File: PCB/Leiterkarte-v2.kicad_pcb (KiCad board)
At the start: 4 copper layers, 69.2 x 70 mm, 59 parts

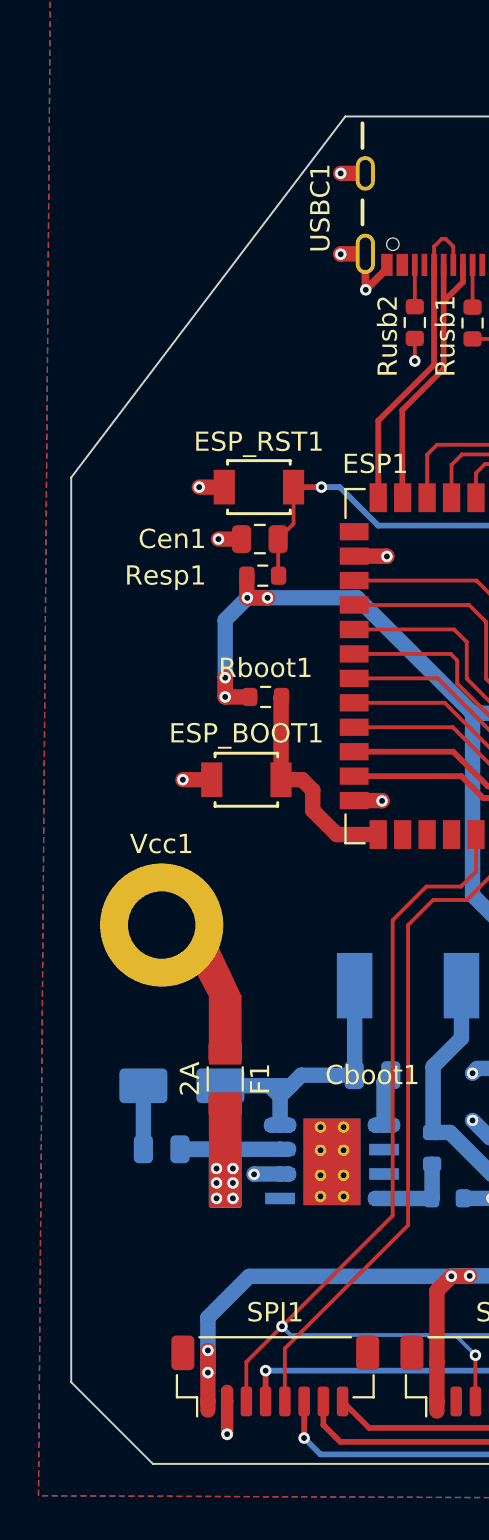
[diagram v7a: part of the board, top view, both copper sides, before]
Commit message: Changed buttons footprint; Changed buttons LCSC component due to shortage; Updated components rotation for JLCPCB;
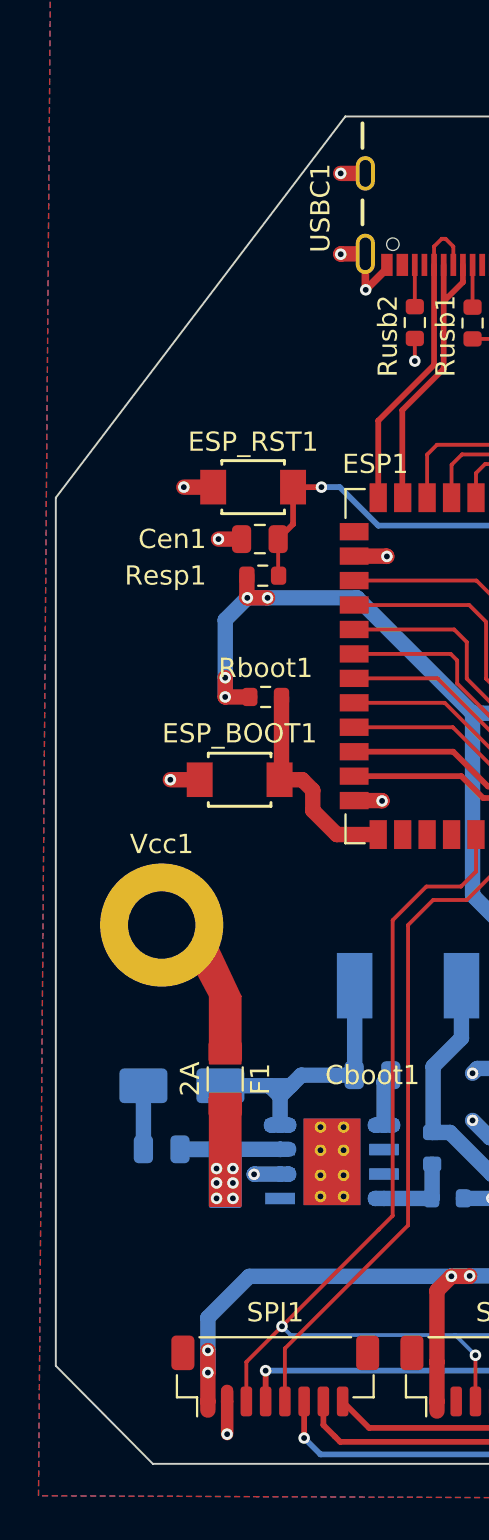
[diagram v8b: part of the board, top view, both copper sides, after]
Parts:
- moved ESP_BOOT1 0.35 mm to (94.3, 82.7)
- moved ESP_RST1 0.30 mm to (95.0, 67.5)
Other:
- board size 69.2 x 70 mm -> 70 x 70 mm
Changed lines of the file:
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@@
 		(tags "resistor")
 		(property "Reference" "Rbtn1"
-			(at 4.325 0 360)
+			(at 4.325 0 0)
 			(layer "F.SilkS")
 			(effects
@@
 		)
 		(property "Value" "10k"
-			(at 0 1.43 360)
+			(at 0 1.43 0)
 			(layer "F.Fab")
 			(effects
@@
 		)
 		(fp_text user "${REFERENCE}"
-			(at 0 0 360)
+			(at 0 0 0)
 			(layer "F.Fab")
 			(effects
@@
 		(tags "resistor")
 		(property "Reference" "Rbtn3"
-			(at -4.35 0 360)
+			(at -4.35 0 0)
 			(layer "F.SilkS")
 			(effects
@@
 		)
 		(property "Value" "10k"
-			(at 0 1.43 360)
+			(at 0 1.43 0)
 			(layer "F.Fab")
 			(effects
@@
 		)
 		(fp_text user "${REFERENCE}"
-			(at 0 0 360)
+			(at 0 0 0)
 			(layer "F.Fab")
 			(effects
@@
 	(footprint "button:small_button"
 		(layer "F.Cu")
-		(at 95.35 67.5)
+		(at 95.05 67.5)
 		(tags "B3U-1000P-B ")
 		(property "Reference" "ESP_RST1"
@@
 		)
 		(fp_line
-			(start -2.55 -1.104)
+			(start -2.9 -1.104)
 			(end -1.754 -1.104)
 			(stroke
@@
 		)
 		(fp_line
-			(start -2.55 1.104)
-			(end -2.55 -1.104)
+			(start -2.9 1.104)
+			(end -2.9 -1.104)
 			(stroke
 				(width 0.1524)
@@
 		)
 		(fp_line
-			(start -2.55 1.104)
+			(start -2.9 1.104)
 			(end -1.754 1.104)
 			(stroke
@@
 		)
 		(fp_line
-			(start 2.55 -1.104)
+			(start 2.9 -1.104)
 			(end 1.754 -1.104)
 			(stroke
@@
 		)
 		(fp_line
-			(start 2.55 -1.104)
-			(end 2.55 1.104)
+			(start 2.9 -1.104)
+			(end 2.9 1.104)
 			(stroke
 				(width 0.1524)
@@
 		)
 		(fp_line
-			(start 2.55 1.104)
+			(start 2.9 1.104)
 			(end 1.754 1.104)
 			(stroke
@@
 		)
 		(pad "1" smd rect
-			(at -1.8 0)
-			(size 1.1 1.8)
+			(at -2.075 0)
+			(size 1.35 1.8)
 			(layers "F.Cu" "F.Paste" "F.Mask")
 			(net 2 "GND")
@@
 		)
 		(pad "2" smd rect
-			(at 1.8 0)
-			(size 1.1 1.8)
+			(at 2.075 0)
+			(size 1.35 1.8)
 			(layers "F.Cu" "F.Paste" "F.Mask")
 			(net 23 "Net-(ESP1-EN)")
@@
 			(pintype "passive")
 		)
-		(model "${KIPRJMOD}/button/small_button.STEP"
-			(offset
-				(xyz 0 0 0)
-			)
-			(scale
-				(xyz 1 1 1)
-			)
-			(rotate
-				(xyz -90 0 0)
-			)
-		)
 	)
 	(footprint "Resistor_SMD:R_0603_1608Metric"
@@
 		(tags "resistor")
 		(property "Reference" "Rbtn2"
-			(at 4.35 0 360)
+			(at 4.35 0 0)
 			(layer "F.SilkS")
 			(effects
@@
 		)
 		(property "Value" "10k"
-			(at 0 1.43 360)
+			(at 0 1.43 0)
 			(layer "F.Fab")
 			(effects
@@
 		)
 		(fp_text user "${REFERENCE}"
-			(at 0 0 360)
+			(at 0 0 0)
 			(layer "F.Fab")
 			(effects
@@
 	(footprint "button:small_button"
 		(layer "F.Cu")
-		(at 94.7 82.7)
+		(at 94.35 82.7)
 		(tags "B3U-1000P-B ")
 		(property "Reference" "ESP_BOOT1"
@@
 		)
 		(fp_line
-			(start -2.55 -1.104)
+			(start -2.9 -1.104)
 			(end -1.754 -1.104)
 			(stroke
@@
 		)
 		(fp_line
-			(start -2.55 1.104)
-			(end -2.55 -1.104)
+			(start -2.9 1.104)
+			(end -2.9 -1.104)
 			(stroke
 				(width 0.1524)
@@
 		)
 		(fp_line
-			(start -2.55 1.104)
+			(start -2.9 1.104)
 			(end -1.754 1.104)
 			(stroke
@@
 		)
 		(fp_line
-			(start 2.55 -1.104)
+			(start 2.9 -1.104)
 			(end 1.754 -1.104)
 			(stroke
@@
 		)
 		(fp_line
-			(start 2.55 -1.104)
-			(end 2.55 1.104)
+			(start 2.9 -1.104)
+			(end 2.9 1.104)
 			(stroke
 				(width 0.1524)
@@
 		)
 		(fp_line
-			(start 2.55 1.104)
+			(start 2.9 1.104)
 			(end 1.754 1.104)
 			(stroke
@@
 		)
 		(pad "1" smd rect
-			(at -1.8 0)
-			(size 1.1 1.8)
+			(at -2.075 0)
+			(size 1.35 1.8)
 			(layers "F.Cu" "F.Paste" "F.Mask")
 			(net 2 "GND")
@@
 		)
 		(pad "2" smd rect
-			(at 1.8 0)
-			(size 1.1 1.8)
+			(at 2.075 0)
+			(size 1.35 1.8)
 			(layers "F.Cu" "F.Paste" "F.Mask")
 			(net 64 "Net-(ESP1-IO0)")
@@
 			(pintype "passive")
 		)
-		(model "${KIPRJMOD}/button/small_button.STEP"
-			(offset
-				(xyz 0 0 0)
-			)
-			(scale
-				(xyz 1 1 1)
-			)
-			(rotate
-				(xyz -90 0 0)
-			)
-		)
 	)
 	(footprint "Resistor_SMD:R_0603_1608Metric"
@@
 	)
 	(gr_line
+		(start 84.8 68.05)
+		(end 84.8 113.15)
+		(stroke
+			(width 0.1)
+			(type default)
+		)
+		(layer "Edge.Cuts")
+	)
+	(gr_line
 		(start 89.842641 118.242641)
 		(end 154.842641 118.242641)
@@
 	)
 	(gr_line
-		(start 85.6 67)
+		(start 84.8 68.05)
 		(end 99.842641 48.242641)
 		(stroke
@@
 	)
 	(gr_line
-		(start 85.6 114)
+		(start 84.8 113.15)
 		(end 89.842641 118.242641)
 		(stroke
@@
 	)
 	(gr_line
-		(start 85.6 114)
-		(end 85.6 67)
-		(stroke
-			(width 0.1)
-			(type default)
-		)
-		(layer "Edge.Cuts")
-	)
-	(gr_line
 		(start 93.6 90.25)
 		(end 93.6 118.25)
@@
 		(layer "User.1")
 	)
+	(gr_line
+		(start 85.6 114)
+		(end 85.6 67)
+		(stroke
+			(width 0.1)
+			(type default)
+		)
+		(layer "User.1")
+	)
 	(gr_text "FOW"
 		(at 149.95 88.25 90)
@@
 	)
 	(segment
-		(start 92.9 82.7)
-		(end 91.4 82.7)
-		(width 0.8)
-		(layer "F.Cu")
-		(net 2)
-	)
-	(segment
 		(start 124.75 76.8)
 		(end 126.2 76.8)
@@
 	)
 	(segment
+		(start 92.275 82.7)
+		(end 90.75 82.7)
+		(width 0.8)
+		(layer "F.Cu")
+		(net 2)
+	)
+	(segment
 		(start 102 56.15)
 		(end 100.9 57.25)
@@
 	)
 	(segment
-		(start 93.55 67.5)
-		(end 92.25 67.5)
-		(width 0.8)
-		(layer "F.Cu")
-		(net 2)
-	)
-	(segment
 		(start 122.3 63.7625)
 		(end 122.3 63.3)
@@
 	)
 	(segment
+		(start 92.975 67.5)
+		(end 91.45 67.5)
+		(width 0.8)
+		(layer "F.Cu")
+		(net 2)
+	)
+	(segment
 		(start 109.52 51.2)
 		(end 108.2 51.2)
@@
 	)
 	(via
-		(at 92.25 67.5)
+		(at 136.95 68)
 		(size 0.6)
 		(drill 0.3)
@@
 	)
 	(via
-		(at 136.95 68)
+		(at 91.45 67.5)
 		(size 0.6)
 		(drill 0.3)
@@
 	)
 	(via
-		(at 91.4 82.7)
+		(at 90.75 82.7)
 		(size 0.6)
 		(drill 0.3)
@@
 	)
 	(segment
-		(start 115.5 69.5)
-		(end 115.5 68.07)
+		(start 97.125 69.425)
+		(end 97.125 67.5)
 		(width 0.3)
 		(layer "F.Cu")
@@
 	)
 	(segment
-		(start 97.15 69.4)
-		(end 97.15 67.5)
-		(width 0.2)
+		(start 115.5 69.5)
+		(end 115.5 68.07)
+		(width 0.3)
 		(layer "F.Cu")
 		(net 23)
 	)
 	(segment
-		(start 115.5 68.07)
-		(end 115.52 68.05)
+		(start 96.35 70.2)
+		(end 97.125 69.425)
 		(width 0.3)
 		(layer "F.Cu")
@@
 	)
 	(segment
-		(start 96.35 72.075)
-		(end 96.375 72.1)
-		(width 0.2)
+		(start 98.6 67.5)
+		(end 97.125 67.5)
+		(width 0.3)
 		(layer "F.Cu")
 		(net 23)
 	)
 	(segment
-		(start 97.15 67.5)
-		(end 98.6 67.5)
+		(start 115.5 68.07)
+		(end 115.52 68.05)
 		(width 0.3)
 		(layer "F.Cu")
@@
 	)
 	(segment
-		(start 96.35 70.2)
-		(end 97.15 69.4)
+		(start 96.35 72.075)
+		(end 96.375 72.1)
 		(width 0.2)
 		(layer "F.Cu")
@@
 	)
 	(segment
-		(start 96.5 82.7)
-		(end 96.5 78.425)
+		(start 98.15 84.3)
+		(end 99.4 85.55)
 		(width 0.8)
 		(layer "F.Cu")
@@
 	)
 	(segment
-		(start 96.5 82.7)
-		(end 97.6 82.7)
+		(start 97.6 82.7)
+		(end 96.425 82.7)
 		(width 0.8)
 		(layer "F.Cu")
@@
 	)
 	(segment
-		(start 96.5 78.425)
-		(end 96.525 78.4)
+		(start 96.525 82.6)
+		(end 96.425 82.7)
 		(width 0.8)
 		(layer "F.Cu")
@@
 	)
 	(segment
-		(start 98.15 84.3)
-		(end 99.4 85.55)
+		(start 99.4 85.55)
+		(end 101.55 85.55)
 		(width 0.8)
 		(layer "F.Cu")
@@
 	)
 	(segment
-		(start 99.4 85.55)
-		(end 101.55 85.55)
+		(start 97.6 82.7)
+		(end 98.15 83.25)
 		(width 0.8)
 		(layer "F.Cu")
@@
 	)
 	(segment
-		(start 97.6 82.7)
-		(end 98.15 83.25)
+		(start 96.525 78.4)
+		(end 96.525 82.6)
 		(width 0.8)
 		(layer "F.Cu")
